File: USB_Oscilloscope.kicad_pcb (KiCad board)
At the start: 4 copper layers, 70 x 43 mm, 110 parts, among them J1 POGO_PROG, J3 DEBUG, P2 HRO TYPE-C-31-M-12, SW1 MSK12C02, U1 LPC4370FET100, U10 USBLC6-2SC6, U11 LM385M3-1.2/TR, U12 LM385M3-1.2/TR, U13 FM24C02B-DN-T-G, U14 MCP4726A0T-E/CH, U15 LM385M3-1.2/TR, U2 CPC1017NTR, U3 MT3406, U4 CPC1017NTR, U5 OPA4354AIPWR, U6 TI LM2664M6X/NOPB, U7 74HC4052PW, U8 ZD25WQ80CEIGR, U9 TC7W53FK, Y1 7E12000E20UCG

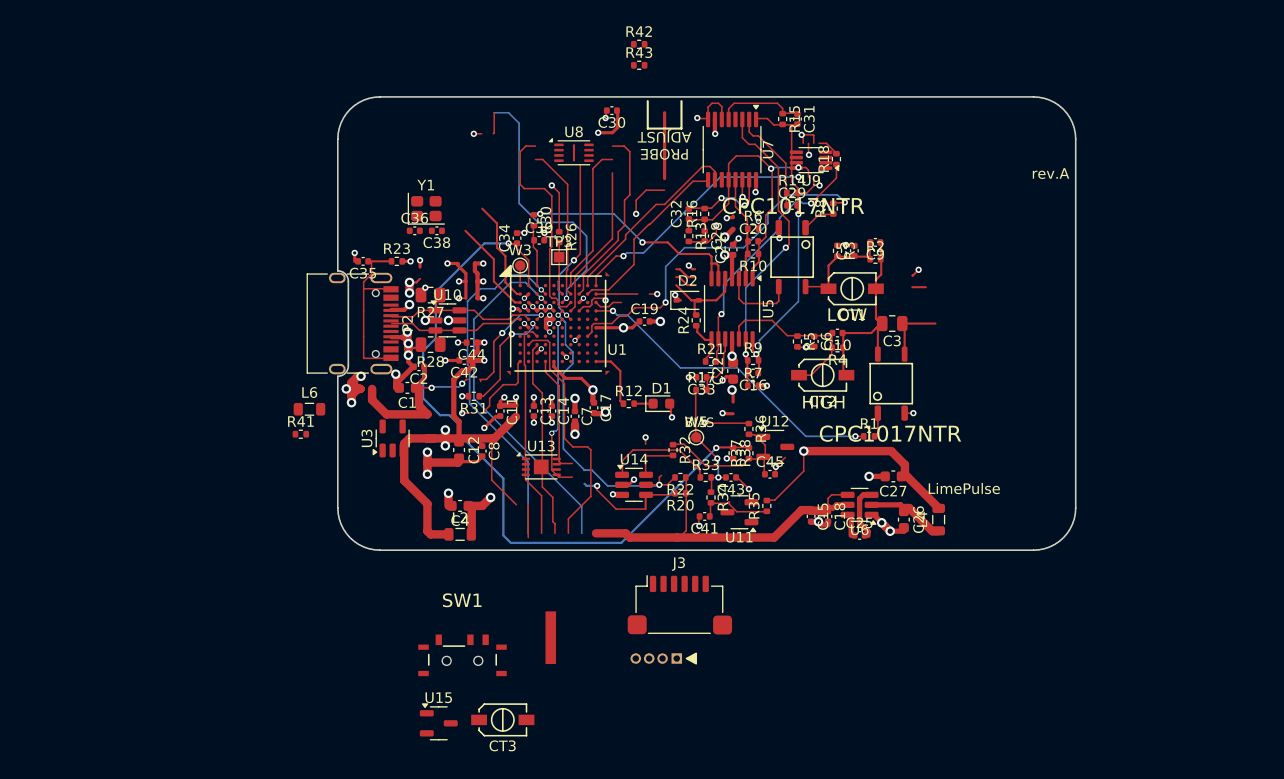
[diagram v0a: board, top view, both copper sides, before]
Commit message: ペン型オシロに変更
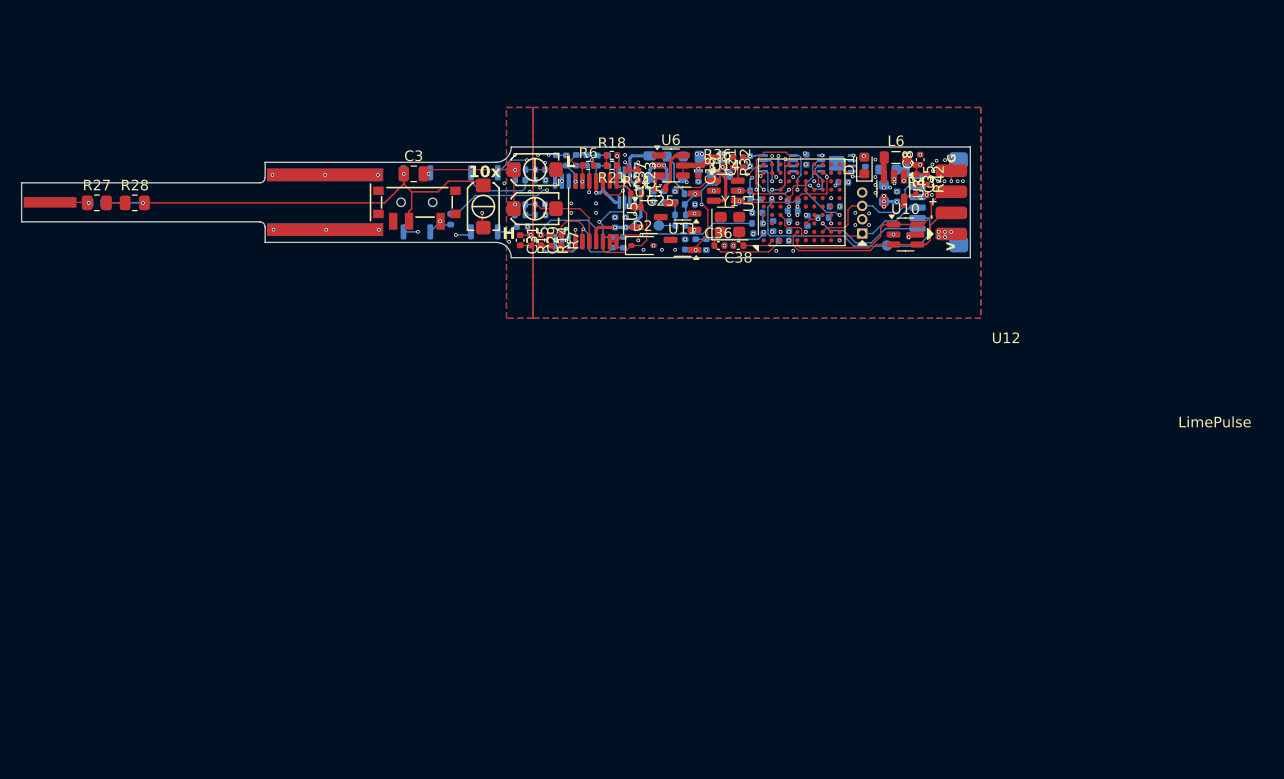
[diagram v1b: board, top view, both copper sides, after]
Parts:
- removed P2: HRO TYPE-C-31-M-12, Connector_USB:USB_C_Receptacle_HRO_TYPE-C-31-M-12
- removed R23, R41: 5.1k 1%, Resistor_SMD:R_0402_1005Metric
- removed W3: ADC1, TestPoint:TestPoint_Pad_D1.0mm
- removed W5: TP_BIAS, TestPoint:TestPoint_Pad_D1.0mm
- added C23: 0.1u, Capacitor_SMD:C_0402_1005Metric, F.Cu at (128.5, 107.5)
- added C24: 0.1u, Capacitor_SMD:C_0402_1005Metric, B.Cu at (126.3, 111.9)
- added C37: 1u, Capacitor_SMD:C_0402_1005Metric, F.Cu at (127.5, 107.5)
- added C40: 1u, Capacitor_SMD:C_0402_1005Metric, B.Cu at (127.3, 111.9)
- added C46: 0.1u, Capacitor_SMD:C_0402_1005Metric, B.Cu at (147.9, 108.1)
- added J2: POGO_PROG, #ps_foot:PIN_HEADER_P1.27x4, F.Cu at (149.8, 111.0)
- added PAD2: SHIELD TUBE, #ps_foot:pipe-out5.0_in4.0_len40.0, F.Cu at (103.1, 110.0)
- added TP2: TP_BIAS, TestPoint:TestPoint_Pad_D1.0mm, B.Cu at (130.4, 112.2)
- C1, C10, C11, C12, C13, C14, C15, C16, C17, C19, C2, C20, C22, C26, C27, C28, C30, C32, C33, C34, C39, C4, C41, C42, C43, C44, C45, C5, C6, C7, C9, J3, L2, L4, R1, R10, R12, R13, R16, R17, R2, R20, R22, R26, R3, R30, R31, R33, R34, R35, R37, R38, R4, R5, R8, R9, U2, U4, U8, U9: moved to B.Cu
- CT1: value STC3MB10-T1 -> STC3MA03-T1; footprint #ps_foot:MURATA_TZC3 -> #ps_foot:SHEWA STC03M
- CT2: value STC3MA03-T1 -> STC3MB10-T1; footprint #ps_foot:MURATA_TZC3 -> #ps_foot:SHEWA STC03M
- CT3: footprint #ps_foot:MURATA_TZC3 -> #ps_foot:SHEWA STC03M
- J1: value POGO_PROG -> Solder pads 1x04; footprint #ps_foot:PIN_HEADER_P1.27x4 -> #ps_foot:01x04_wire_pads_Pitch2.0
- SW1: value MSK12C02 -> MSS12C02LS-BB2.0; footprint #ps_foot:MSK12C02 -> #ps_foot:MSS12C02LS-BB2.0
- TP3: footprint TestPoint:TestPoint_Pad_1.0x1.0mm -> TestPoint:TestPoint_Pad_D1.0mm; moved to B.Cu
- U1: footprint MyIC:TFBGA100_MYREFLOW -> Package_BGA:TFBGA-100_8x8mm_Layout10x10_P0.8mm
- U13: footprint Package_DFN_QFN:TDFN-8-1EP_3x2mm_P0.5mm_EP1.4x1.4mm -> #ps_foot:TDFN-8-1EP_3x2mm_P0.5mm_EP1.4x1.4mm; moved to B.Cu
- U7: value 74HC4052PW -> 74HC4052PW,118; moved to B.Cu
- moved PAD1 62.9 mm to (72.7, 110.0), turned to -90 degrees
- moved C22 62.4 mm to (77.1, 110.0), turned to 180 degrees
- moved L6 60.5 mm to (152.9, 105.8)
- moved U3 53.1 mm to (152.7, 108.7), turned to -90 degrees
- moved C35 53.1 mm to (154.9, 107.8), turned to -90 degrees
- moved U15 52.0 mm to (129.5, 111.4)
- moved J1 51.5 mm to (158.2, 110.0), turned to 90 degrees
- moved C8 49.9 mm to (155.2, 106.0), turned to 90 degrees
- moved C1 48.8 mm to (151.8, 109.1), turned to 90 degrees
- moved C12 48.6 mm to (152.2, 106.9), turned to 180 degrees
- moved CT3 48.6 mm to (118.7, 110.6)
- moved U2 48.2 mm to (107.5, 110.0), turned to 180 degrees
- moved C2 48.1 mm to (153.1, 109.5), turned to 90 degrees
- moved C3 47.6 mm to (107.2, 107.3), turned to 0 degrees
- moved J3 45.4 mm to (157.0, 110.0), turned to -90 degrees
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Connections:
- C10 pad 1: Net-(U2-INOUT1) -> /DIV_IN_40V
- C10 pad 2: /HIGH_VDIV -> /H_DIV
- C16 pad 1: Net-(U5D-OUT) -> /H_OP_OUT
- C16 pad 2: Net-(U5D--IN) -> /H_OP-
- C20 pad 1: Net-(U5A--IN) -> /L_OP-
- C20 pad 2: Net-(U5A-OUT) -> /L_OP_OUT
- C22 pad 1: Net-(SW1-A) -> /DCC_IN_40V
- C22 pad 2: Net-(PAD1-Pin_1) -> /TIP_400V
- C28 pad 1: Net-(U5A-OUT) -> /L_OP_OUT
- C29 pad 2: Net-(U5D-OUT) -> /H_OP_OUT
- C3 pad 1: Net-(SW1-A) -> /DCC_IN_40V
- C3 pad 2: Net-(U2-INOUT1) -> /DIV_IN_40V
- C31 pad 2: Net-(U5D-OUT) -> /H_OP_OUT
- C32 pad 1: Net-(U5A-OUT) -> /L_OP_OUT
- C33 pad 1: Net-(U5C-+IN) -> /OP_CLP+
- C5 pad 1: /LOW_VDIV -> /L_DIV
- C6 pad 1: /HIGH_VDIV -> /H_DIV
- C9 pad 1: Net-(U2-INOUT1) -> /DIV_IN_40V
- C9 pad 2: /LOW_VDIV -> /L_DIV
- CT1 pad 1: Net-(U2-INOUT1) -> /TIP_400V
- CT1 pad 2: /LOW_VDIV -> /DCC_IN_40V
- CT2 pad 1: Net-(U2-INOUT1) -> /L_DIV
- CT2 pad 2: /HIGH_VDIV -> /DIV_IN_40V
- CT3 pad 1: Net-(PAD1-Pin_1) -> /H_DIV
- CT3 pad 2: Net-(SW1-A) -> /DIV_IN_40V
- D2 pad 1: Net-(D2-K) -> /OP_VF+
- J1 pad 1: /SWDIO -> /USB_VBUS
- J1 pad 2: GND -> /USB_D-
- J1 pad 3: /SWCLK -> /USB_D+
- J1 pad 4: VDD -> GND
- PAD1 pad 1: Net-(PAD1-Pin_1) -> /TIP_400V
- R10 pad 1: Net-(U5A-OUT) -> /L_OP_OUT
- R10 pad 2: Net-(U5A--IN) -> /L_OP-
- R13 pad 1: Net-(U5A-OUT) -> /L_OP_OUT
- R14 pad 2: Net-(U5D-OUT) -> /H_OP_OUT
- R15 pad 2: Net-(U5D-OUT) -> /H_OP_OUT
- R16 pad 1: Net-(U5A-OUT) -> /L_OP_OUT
- R17 pad 2: Net-(U5C-+IN) -> /OP_CLP+
- R18 pad 1: Net-(U5C--IN) -> /OP_CLP-
- R2 pad 1: /LOW_VDIV -> /L_DIV
- R2 pad 2: Net-(U2-INOUT1) -> /DIV_IN_40V
- R21 pad 1: Net-(U5C-OUT) -> Net-(U5A-OUT)
- R21 pad 2: Net-(U5C--IN) -> /OP_CLP-
- R24 pad 1: Net-(U5C-OUT) -> Net-(U5A-OUT)
- R24 pad 2: Net-(D2-K) -> /OP_VF+
- R27 pad 1: Net-(PAD1-Pin_1) -> /TIP_400V
- R28 pad 2: Net-(SW1-A) -> /DCC_IN_40V
- R3 pad 2: /LOW_VDIV -> /L_DIV
- R30 pad 1: Net-(U5B--IN) -> /OP_VF-
- R4 pad 1: Net-(U2-INOUT1) -> /DIV_IN_40V
- R4 pad 2: /HIGH_VDIV -> /H_DIV
- R5 pad 1: /HIGH_VDIV -> /H_DIV
- R6 pad 1: Net-(U5A--IN) -> /L_OP-
- R7 pad 1: Net-(U5D--IN) -> /H_OP-
- R9 pad 1: Net-(U5D--IN) -> /H_OP-
- R9 pad 2: Net-(U5D-OUT) -> /H_OP_OUT
- SW1 pad 1: Net-(SW1-A) -> /TIP_400V
- SW1 pad 2: Net-(PAD1-Pin_1) -> /DCC_IN_40V
- SW1 pad S1: GND -> unconnected-(SW1-PadS1)
- SW1 pad S2: GND -> unconnected-(SW1-PadS2)
- SW1 pad S3: GND -> unconnected-(SW1-PadS3)
- SW1 pad S4: GND -> unconnected-(SW1-PadS4)
- U1 pad A1: Net-(U1B-ADC1) -> unconnected-(U1B-ADC1-PadA1)
- U10 pad 1: /USB_D- -> /USB_D+
- U10 pad 3: /USB_D+ -> /USB_D-
- U10 pad 4: /USB_D+ -> /USB_D-
- U10 pad 6: /USB_D- -> /USB_D+
- U15 pad 1: Net-(D2-K) -> /OP_VF+
- U2 pad 3: Net-(SW1-A) -> /DCC_IN_40V
- U2 pad 4: Net-(U2-INOUT1) -> /DIV_IN_40V
- U4 pad 3: /LOW_VDIV -> /L_DIV
- U4 pad 4: Net-(U4-INOUT1) -> /L_OP+
- U5 pad 10: Net-(U5C-+IN) -> /H_DIV
- U5 pad 12: /HIGH_VDIV -> /OP_VF+
- U5 pad 13: Net-(U5D--IN) -> /OP_VF-
- U5 pad 14: Net-(U5D-OUT) -> /OP_VF-
- U5 pad 2: Net-(U5A--IN) -> /OP_CLP-
- U5 pad 3: Net-(U4-INOUT1) -> /OP_CLP+
- U5 pad 5: Net-(D2-K) -> /L_OP+
- U5 pad 6: Net-(U5B--IN) -> /L_OP-
- U5 pad 7: Net-(U5B--IN) -> /L_OP_OUT
- U5 pad 8: Net-(U5C-OUT) -> /H_OP_OUT
- U5 pad 9: Net-(U5C--IN) -> /H_OP-
- U7 pad 1: Net-(U5D-OUT) -> /H_OP_OUT
- U7 pad 12: Net-(U5A-OUT) -> /L_OP_OUT
- U7 pad 13: Net-(U5A--IN) -> /L_OP-
- U7 pad 3: Net-(U5D--IN) -> /H_OP-
- U9 pad 6: Net-(U5A-OUT) -> /L_OP_OUT
- U9 pad 7: Net-(U5D-OUT) -> /H_OP_OUT
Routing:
- net (no net): track 269.9 -> 0.00 mm, vias 9 -> 0
- net GND: track 172.1 -> 6.97 mm, vias 60 -> 98
- net /ADCHS_VPOS0: track 68.6 -> 6.63 mm, vias 2 -> 1
- net alt_VAA-: track 82.8 -> 26.7 mm, vias 6 -> 3
- net alt_VAA+: track 77.7 -> 27.4 mm
- net /TIP_400V: track 0.00 -> 44.0 mm, vias 0 -> 3
- net /DCC_IN_40V: track 0.00 -> 41.5 mm, vias 0 -> 2
- net Net-(U4-ANOD): track 38.2 -> 2.03 mm, vias 2 -> 0
- net Net-(U5D-OUT): track 34.1 -> 0.00 mm, vias 2 -> 0
- net unconnected-(U1B-TRST#-PadB4): track 33.6 -> 0.00 mm, vias 1 -> 0
- net /OP_LOW_SW: track 0.00 -> 31.3 mm, vias 0 -> 2
- net Net-(U5D--IN): track 30.6 -> 0.00 mm, vias 2 -> 0
- net Net-(U5A-OUT): track 30.7 -> 3.20 mm, vias 2 -> 0
- net VDD: track 86.3 -> 60.3 mm, vias 24 -> 22
- net Net-(U5C--IN): track 24.4 -> 0.00 mm, vias 2 -> 0
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- added copper zone on B.Cu, net GND
- added copper zone on F.Cu, net GND
- added copper zone on In1.Cu, net GND
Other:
- board size 70 x 43 mm -> 90 x 10.5 mm
- rule pad_to_mask_clearance: 0.15 -> 0
- board text added: "+"
- board text added: "-"
- board text added: "10x"
- board text added: "G"
- board text added: "H"
- board text added: "L"
- board text added: "V"
- board text removed: "BIAS"
- board text removed: "Eco1 = Acrylic Cover TOP Eco2 = Acrylic Cover Bottom"
- board text removed: "HIGH"
- board text removed: "LOW"
- board text removed: "PROBE ADJUST"
- board text removed: "QRCode contains URL of host application"
- board text removed: "rev.A"
